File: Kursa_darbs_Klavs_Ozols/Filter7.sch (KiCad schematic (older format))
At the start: 11 parts, among them U9 TL074

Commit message: Shii ir 2. iteraacija kursa darbam!
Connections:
- net Audio4.5kHz: now also R42.1; no longer R42.2
- net at C36.1, R40.2, U9.1: now also R39.1; no longer R39.2
- net at C35.1, U9.2 (-): now also R39.2; no longer R39.1
- net at C37.1, U9.6 (-): now also R42.2; no longer R42.1
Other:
- moved on the sheet: R38, R41
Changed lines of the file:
@@
 L R R38
 U 1 1 5B01AED2
-P 2050 2500
-F 0 "R38" V 2130 2500 50  0000 C CNN
-F 1 "5.1k" V 2050 2500 50  0000 C CNN
-F 2 "" V 1980 2500 50  0001 C CNN
-F 3 "" H 2050 2500 50  0001 C CNN
-	1    2050 2500
+P 2050 2550
+F 0 "R38" V 2130 2550 50  0000 C CNN
+F 1 "5.1k" V 2050 2550 50  0000 C CNN
+F 2 "" V 1980 2550 50  0001 C CNN
+F 3 "" H 2050 2550 50  0001 C CNN
+	1    2050 2550
 	1    0    0    -1
 $EndComp
@@
 F 3 "" H 2750 2900 50  0001 C CNN
 	1    2750 2900
-	1    0    0    -1
+	0    1    1    0
 $EndComp
 Text HLabel 1450 2350 0    60   Input ~ 0
@@
 L R R41
 U 1 1 5B01B48F
-P 4400 2400
-F 0 "R41" V 4480 2400 50  0000 C CNN
-F 1 "5.1k" V 4400 2400 50  0000 C CNN
-F 2 "" V 4330 2400 50  0001 C CNN
-F 3 "" H 4400 2400 50  0001 C CNN
-	1    4400 2400
+P 4400 2450
+F 0 "R41" V 4480 2450 50  0000 C CNN
+F 1 "5.1k" V 4400 2450 50  0000 C CNN
+F 2 "" V 4330 2450 50  0001 C CNN
+F 3 "" H 4400 2450 50  0001 C CNN
+	1    4400 2450
 	1    0    0    -1
 $EndComp
@@
 F 3 "" H 5100 2800 50  0001 C CNN
 	1    5100 2800
-	1    0    0    -1
+	0    1    1    0
 $EndComp
 $Comp
@@
 	2550 3100 3700 3100
 Wire Wire Line
-	2750 3100 2750 3050
-Wire Wire Line
-	2250 3100 2050 3100
-Wire Wire Line
-	2050 3100 2050 2650
+	2750 3000 2750 3100
+Wire Wire Line
+	2050 3100 2250 3100
 Wire Wire Line
 	1950 2750 2250 2750
@@
 	4900 3000 6050 3000
 Wire Wire Line
-	5100 3000 5100 2950
-Wire Wire Line
-	4600 3000 4400 3000
-Wire Wire Line
-	4400 3000 4400 2550
+	5100 2900 5100 3000
+Wire Wire Line
+	4400 3000 4600 3000
 Wire Wire Line
 	4300 2650 4600 2650
@@
 	2300 2000 2300 2100
 Connection ~ 2300 2100
+Wire Wire Line
+	4400 2300 4400 2250
+Wire Wire Line
+	4400 2600 4400 3000
+Wire Wire Line
+	4950 2800 4950 2700
+Wire Wire Line
+	4950 2700 5100 2700
+Wire Wire Line
+	5100 2700 5100 2650
+Wire Wire Line
+	5250 2800 5250 2900
+Wire Wire Line
+	5250 2900 5100 2900
+Wire Wire Line
+	2600 2900 2600 2800
+Wire Wire Line
+	2600 2800 2750 2800
+Wire Wire Line
+	2750 2800 2750 2750
+Wire Wire Line
+	2900 2900 2900 3000
+Wire Wire Line
+	2900 3000 2750 3000
+Wire Wire Line
+	2050 2350 2050 2400
+Wire Wire Line
+	2050 2700 2050 3100
 $EndSCHEMATC

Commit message: Shii ir kursa darba 3. iteraacija
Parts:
- C35, C36, C37, C38: footprint (none) -> Capacitors_THT:C_Axial_L5.1mm_D3.1mm_P10.00mm_Horizontal
- R37, R38, R39, R40, R41, R42: footprint (none) -> Resistors_THT:R_Axial_DIN0309_L9.0mm_D3.2mm_P5.08mm_Vertical
- U9: footprint (none) -> TL074:DIL14
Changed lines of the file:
@@
 F 0 "U9" H 3250 2850 50  0000 L CNN
 F 1 "TL074" H 3250 2450 50  0000 L CNN
-F 2 "" H 3200 2750 50  0001 C CNN
+F 2 "TL074:DIL14" H 3200 2750 50  0001 C CNN
 F 3 "" H 3300 2850 50  0001 C CNN
 	1    3250 2650
@@
 F 0 "R37" V 1880 2750 50  0000 C CNN
 F 1 "6.8k" V 1800 2750 50  0000 C CNN
-F 2 "" V 1730 2750 50  0001 C CNN
-F 3 "" H 1800 2750 50  0001 C CNN
+F 2 "Resistors_THT:R_Axial_DIN0309_L9.0mm_D3.2mm_P5.08mm_Vertical" V 1730 2750 50  0001 C CNN
+F 3 "https://eu.mouser.com/datasheet/2/219/MOS-16613.pdf" H 1800 2750 50  0001 C CNN
 	1    1800 2750
 	0    1    1    0
@@
 F 0 "R38" V 2130 2550 50  0000 C CNN
 F 1 "5.1k" V 2050 2550 50  0000 C CNN
-F 2 "" V 1980 2550 50  0001 C CNN
-F 3 "" H 2050 2550 50  0001 C CNN
+F 2 "Resistors_THT:R_Axial_DIN0309_L9.0mm_D3.2mm_P5.08mm_Vertical" V 1980 2550 50  0001 C CNN
+F 3 "https://eu.mouser.com/datasheet/2/219/MOS-16613.pdf" H 2050 2550 50  0001 C CNN
 	1    2050 2550
 	1    0    0    -1
@@
 F 0 "C35" H 2425 2850 50  0000 L CNN
 F 1 "2.2nF" H 2425 2650 50  0000 L CNN
-F 2 "" H 2438 2600 50  0001 C CNN
-F 3 "" H 2400 2750 50  0001 C CNN
+F 2 "Capacitors_THT:C_Axial_L5.1mm_D3.1mm_P10.00mm_Horizontal" H 2438 2600 50  0001 C CNN
+F 3 "https://eu.mouser.com/datasheet/2/212/KEM_C1046_AXIAL_MOLDED_X7R-1145195.pdf" H 2400 2750 50  0001 C CNN
 	1    2400 2750
 	0    1    1    0
@@
 F 0 "C36" H 2425 3200 50  0000 L CNN
 F 1 "2.2nF" H 2425 3000 50  0000 L CNN
-F 2 "" H 2438 2950 50  0001 C CNN
-F 3 "" H 2400 3100 50  0001 C CNN
+F 2 "Capacitors_THT:C_Axial_L5.1mm_D3.1mm_P10.00mm_Horizontal" H 2438 2950 50  0001 C CNN
+F 3 "https://eu.mouser.com/datasheet/2/212/KEM_C1046_AXIAL_MOLDED_X7R-1145195.pdf" H 2400 3100 50  0001 C CNN
 	1    2400 3100
 	0    1    1    0
@@
 F 0 "R39" V 2830 2900 50  0000 C CNN
 F 1 "62k" V 2750 2900 50  0000 C CNN
-F 2 "" V 2680 2900 50  0001 C CNN
-F 3 "" H 2750 2900 50  0001 C CNN
+F 2 "Resistors_THT:R_Axial_DIN0309_L9.0mm_D3.2mm_P5.08mm_Vertical" V 2680 2900 50  0001 C CNN
+F 3 "https://eu.mouser.com/datasheet/2/219/MOS-16613.pdf" H 2750 2900 50  0001 C CNN
 	1    2750 2900
 	0    1    1    0
@@
 F 0 "R40" V 4230 2650 50  0000 C CNN
 F 1 "6.8k" V 4150 2650 50  0000 C CNN
-F 2 "" V 4080 2650 50  0001 C CNN
-F 3 "" H 4150 2650 50  0001 C CNN
+F 2 "Resistors_THT:R_Axial_DIN0309_L9.0mm_D3.2mm_P5.08mm_Vertical" V 4080 2650 50  0001 C CNN
+F 3 "https://eu.mouser.com/datasheet/2/219/MOS-16613.pdf" H 4150 2650 50  0001 C CNN
 	1    4150 2650
 	0    1    1    0
@@
 F 0 "R41" V 4480 2450 50  0000 C CNN
 F 1 "5.1k" V 4400 2450 50  0000 C CNN
-F 2 "" V 4330 2450 50  0001 C CNN
-F 3 "" H 4400 2450 50  0001 C CNN
+F 2 "Resistors_THT:R_Axial_DIN0309_L9.0mm_D3.2mm_P5.08mm_Vertical" V 4330 2450 50  0001 C CNN
+F 3 "https://eu.mouser.com/datasheet/2/219/MOS-16613.pdf" H 4400 2450 50  0001 C CNN
 	1    4400 2450
 	1    0    0    -1
@@
 F 0 "C37" H 4775 2750 50  0000 L CNN
 F 1 "2.2nF" H 4775 2550 50  0000 L CNN
-F 2 "" H 4788 2500 50  0001 C CNN
-F 3 "" H 4750 2650 50  0001 C CNN
+F 2 "Capacitors_THT:C_Axial_L5.1mm_D3.1mm_P10.00mm_Horizontal" H 4788 2500 50  0001 C CNN
+F 3 "https://eu.mouser.com/datasheet/2/212/KEM_C1046_AXIAL_MOLDED_X7R-1145195.pdf" H 4750 2650 50  0001 C CNN
 	1    4750 2650
 	0    1    1    0
@@
 F 0 "C38" H 4775 3100 50  0000 L CNN
 F 1 "2.2nF" H 4775 2900 50  0000 L CNN
-F 2 "" H 4788 2850 50  0001 C CNN
-F 3 "" H 4750 3000 50  0001 C CNN
+F 2 "Capacitors_THT:C_Axial_L5.1mm_D3.1mm_P10.00mm_Horizontal" H 4788 2850 50  0001 C CNN
+F 3 "https://eu.mouser.com/datasheet/2/212/KEM_C1046_AXIAL_MOLDED_X7R-1145195.pdf" H 4750 3000 50  0001 C CNN
 	1    4750 3000
 	0    1    1    0
@@
 F 0 "R42" V 5180 2800 50  0000 C CNN
 F 1 "62k" V 5100 2800 50  0000 C CNN
-F 2 "" V 5030 2800 50  0001 C CNN
-F 3 "" H 5100 2800 50  0001 C CNN
+F 2 "Resistors_THT:R_Axial_DIN0309_L9.0mm_D3.2mm_P5.08mm_Vertical" V 5030 2800 50  0001 C CNN
+F 3 "https://eu.mouser.com/datasheet/2/219/MOS-16613.pdf" H 5100 2800 50  0001 C CNN
 	1    5100 2800
 	0    1    1    0
@@
 F 0 "U9" H 5600 2750 50  0000 L CNN
 F 1 "TL074" H 5600 2350 50  0000 L CNN
-F 2 "" H 5550 2650 50  0001 C CNN
+F 2 "TL074:DIL14" H 5550 2650 50  0001 C CNN
 F 3 "" H 5650 2750 50  0001 C CNN
 	2    5600 2550

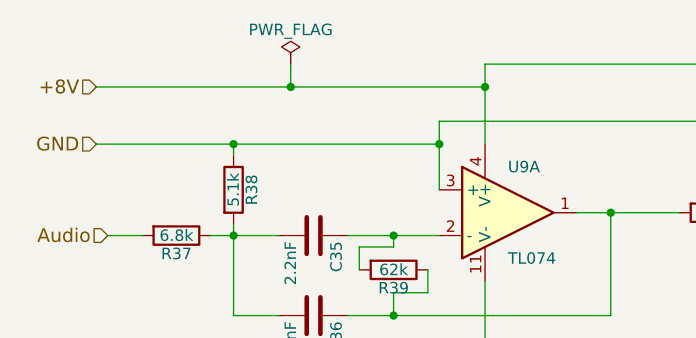
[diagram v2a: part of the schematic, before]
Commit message: Kursa darba plates 4. iteraacija
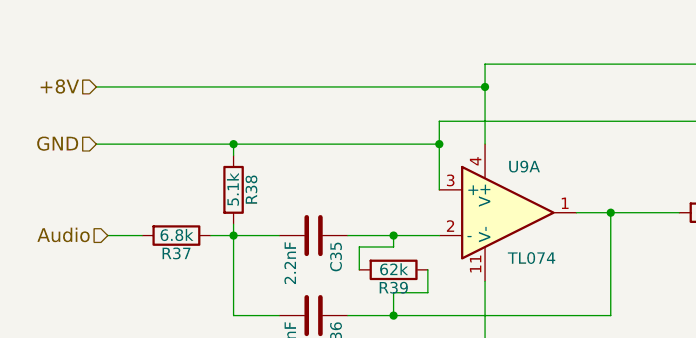
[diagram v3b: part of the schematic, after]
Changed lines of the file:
@@
 Text HLabel 6500 2550 2    60   Output ~ 0
 Audio4.5kHz
-$Comp
-L PWR_FLAG #FLG04
-U 1 1 5B046DF8
-P 2300 2000
-F 0 "#FLG04" H 2300 2075 50  0001 C CNN
-F 1 "PWR_FLAG" H 2300 2150 50  0000 C CNN
-F 2 "" H 2300 2000 50  0001 C CNN
-F 3 "" H 2300 2000 50  0001 C CNN
-	1    2300 2000
-	1    0    0    -1
-$EndComp
-Wire Wire Line
-	2300 2000 2300 2100
-Connection ~ 2300 2100
 Wire Wire Line
 	4400 2300 4400 2250

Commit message: Shiii ir 5. iteraacija manai platei - layouts
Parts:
- C35, C36, C37, C38: footprint Capacitors_THT:C_Axial_L5.1mm_D3.1mm_P10.00mm_Horizontal -> Capacitors_SMD:C_0805_HandSoldering
- R37, R38, R39, R40, R41, R42: footprint Resistors_THT:R_Axial_DIN0309_L9.0mm_D3.2mm_P5.08mm_Vertical -> Resistors_SMD:R_0805_HandSoldering
- U9: footprint TL074:DIL14 -> TL074:SO14
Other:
- moved on the sheet: C36, C38, R39, R42
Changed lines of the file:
@@
 EESchema Schematic File Version 2
+LIBS:Kursa_darbs_Klavs_Ozols-rescue
 LIBS:power
 LIBS:device
@@
 F 0 "U9" H 3250 2850 50  0000 L CNN
 F 1 "TL074" H 3250 2450 50  0000 L CNN
-F 2 "TL074:DIL14" H 3200 2750 50  0001 C CNN
+F 2 "TL074:SO14" H 3200 2750 50  0001 C CNN
 F 3 "" H 3300 2850 50  0001 C CNN
 	1    3250 2650
@@
 F 0 "R37" V 1880 2750 50  0000 C CNN
 F 1 "6.8k" V 1800 2750 50  0000 C CNN
-F 2 "Resistors_THT:R_Axial_DIN0309_L9.0mm_D3.2mm_P5.08mm_Vertical" V 1730 2750 50  0001 C CNN
-F 3 "https://eu.mouser.com/datasheet/2/219/MOS-16613.pdf" H 1800 2750 50  0001 C CNN
+F 2 "Resistors_SMD:R_0805_HandSoldering" V 1730 2750 50  0001 C CNN
+F 3 "https://eu.mouser.com/datasheet/2/219/RN73-11994.pdf" H 1800 2750 50  0001 C CNN
 	1    1800 2750
 	0    1    1    0
@@
 F 0 "R38" V 2130 2550 50  0000 C CNN
 F 1 "5.1k" V 2050 2550 50  0000 C CNN
-F 2 "Resistors_THT:R_Axial_DIN0309_L9.0mm_D3.2mm_P5.08mm_Vertical" V 1980 2550 50  0001 C CNN
-F 3 "https://eu.mouser.com/datasheet/2/219/MOS-16613.pdf" H 2050 2550 50  0001 C CNN
+F 2 "Resistors_SMD:R_0805_HandSoldering" V 1980 2550 50  0001 C CNN
+F 3 "https://eu.mouser.com/datasheet/2/219/RN73-11994.pdf" H 2050 2550 50  0001 C CNN
 	1    2050 2550
 	1    0    0    -1
@@
 F 0 "C35" H 2425 2850 50  0000 L CNN
 F 1 "2.2nF" H 2425 2650 50  0000 L CNN
-F 2 "Capacitors_THT:C_Axial_L5.1mm_D3.1mm_P10.00mm_Horizontal" H 2438 2600 50  0001 C CNN
-F 3 "https://eu.mouser.com/datasheet/2/212/KEM_C1046_AXIAL_MOLDED_X7R-1145195.pdf" H 2400 2750 50  0001 C CNN
+F 2 "Capacitors_SMD:C_0805_HandSoldering" H 2438 2600 50  0001 C CNN
+F 3 "https://eu.mouser.com/datasheet/2/427/vjcommercialseries-222796.pdf" H 2400 2750 50  0001 C CNN
 	1    2400 2750
 	0    1    1    0
@@
 L C C36
 U 1 1 5B01AF60
-P 2400 3100
-F 0 "C36" H 2425 3200 50  0000 L CNN
-F 1 "2.2nF" H 2425 3000 50  0000 L CNN
-F 2 "Capacitors_THT:C_Axial_L5.1mm_D3.1mm_P10.00mm_Horizontal" H 2438 2950 50  0001 C CNN
-F 3 "https://eu.mouser.com/datasheet/2/212/KEM_C1046_AXIAL_MOLDED_X7R-1145195.pdf" H 2400 3100 50  0001 C CNN
-	1    2400 3100
+P 2400 3350
+F 0 "C36" H 2425 3450 50  0000 L CNN
+F 1 "2.2nF" H 2425 3250 50  0000 L CNN
+F 2 "Capacitors_SMD:C_0805_HandSoldering" H 2438 3200 50  0001 C CNN
+F 3 "https://eu.mouser.com/datasheet/2/427/vjcommercialseries-222796.pdf" H 2400 3350 50  0001 C CNN
+	1    2400 3350
 	0    1    1    0
 $EndComp
@@
 L R R39
 U 1 1 5B01B098
-P 2750 2900
-F 0 "R39" V 2830 2900 50  0000 C CNN
-F 1 "62k" V 2750 2900 50  0000 C CNN
-F 2 "Resistors_THT:R_Axial_DIN0309_L9.0mm_D3.2mm_P5.08mm_Vertical" V 2680 2900 50  0001 C CNN
-F 3 "https://eu.mouser.com/datasheet/2/219/MOS-16613.pdf" H 2750 2900 50  0001 C CNN
-	1    2750 2900
-	0    1    1    0
+P 2750 3000
+F 0 "R39" V 2830 3000 50  0000 C CNN
+F 1 "62k" V 2750 3000 50  0000 C CNN
+F 2 "Resistors_SMD:R_0805_HandSoldering" V 2680 3000 50  0001 C CNN
+F 3 "https://eu.mouser.com/datasheet/2/219/RN73-11994.pdf" H 2750 3000 50  0001 C CNN
+	1    2750 3000
+	-1   0    0    1
 $EndComp
 Text HLabel 1450 2350 0    60   Input ~ 0
@@
 Text HLabel 1450 2100 0    60   Input ~ 0
 +8V
-Text HLabel 1500 3450 0    60   Input ~ 0
+Text HLabel 1500 3700 0    60   Input ~ 0
 -8V
 $Comp
@@
 F 0 "R40" V 4230 2650 50  0000 C CNN
 F 1 "6.8k" V 4150 2650 50  0000 C CNN
-F 2 "Resistors_THT:R_Axial_DIN0309_L9.0mm_D3.2mm_P5.08mm_Vertical" V 4080 2650 50  0001 C CNN
-F 3 "https://eu.mouser.com/datasheet/2/219/MOS-16613.pdf" H 4150 2650 50  0001 C CNN
+F 2 "Resistors_SMD:R_0805_HandSoldering" V 4080 2650 50  0001 C CNN
+F 3 "https://eu.mouser.com/datasheet/2/219/RN73-11994.pdf" H 4150 2650 50  0001 C CNN
 	1    4150 2650
 	0    1    1    0
@@
 F 0 "R41" V 4480 2450 50  0000 C CNN
 F 1 "5.1k" V 4400 2450 50  0000 C CNN
-F 2 "Resistors_THT:R_Axial_DIN0309_L9.0mm_D3.2mm_P5.08mm_Vertical" V 4330 2450 50  0001 C CNN
-F 3 "https://eu.mouser.com/datasheet/2/219/MOS-16613.pdf" H 4400 2450 50  0001 C CNN
+F 2 "Resistors_SMD:R_0805_HandSoldering" V 4330 2450 50  0001 C CNN
+F 3 "https://eu.mouser.com/datasheet/2/219/RN73-11994.pdf" H 4400 2450 50  0001 C CNN
 	1    4400 2450
 	1    0    0    -1
@@
 F 0 "C37" H 4775 2750 50  0000 L CNN
 F 1 "2.2nF" H 4775 2550 50  0000 L CNN
-F 2 "Capacitors_THT:C_Axial_L5.1mm_D3.1mm_P10.00mm_Horizontal" H 4788 2500 50  0001 C CNN
-F 3 "https://eu.mouser.com/datasheet/2/212/KEM_C1046_AXIAL_MOLDED_X7R-1145195.pdf" H 4750 2650 50  0001 C CNN
+F 2 "Capacitors_SMD:C_0805_HandSoldering" H 4788 2500 50  0001 C CNN
+F 3 "https://eu.mouser.com/datasheet/2/427/vjcommercialseries-222796.pdf" H 4750 2650 50  0001 C CNN
 	1    4750 2650
 	0    1    1    0
@@
 L C C38
 U 1 1 5B01B49B
-P 4750 3000
-F 0 "C38" H 4775 3100 50  0000 L CNN
-F 1 "2.2nF" H 4775 2900 50  0000 L CNN
-F 2 "Capacitors_THT:C_Axial_L5.1mm_D3.1mm_P10.00mm_Horizontal" H 4788 2850 50  0001 C CNN
-F 3 "https://eu.mouser.com/datasheet/2/212/KEM_C1046_AXIAL_MOLDED_X7R-1145195.pdf" H 4750 3000 50  0001 C CNN
-	1    4750 3000
+P 4750 3250
+F 0 "C38" H 4775 3350 50  0000 L CNN
+F 1 "2.2nF" H 4775 3150 50  0000 L CNN
+F 2 "Capacitors_SMD:C_0805_HandSoldering" H 4788 3100 50  0001 C CNN
+F 3 "https://eu.mouser.com/datasheet/2/427/vjcommercialseries-222796.pdf" H 4750 3250 50  0001 C CNN
+	1    4750 3250
 	0    1    1    0
 $EndComp
@@
 L R R42
 U 1 1 5B01B4A1
-P 5100 2800
-F 0 "R42" V 5180 2800 50  0000 C CNN
-F 1 "62k" V 5100 2800 50  0000 C CNN
-F 2 "Resistors_THT:R_Axial_DIN0309_L9.0mm_D3.2mm_P5.08mm_Vertical" V 5030 2800 50  0001 C CNN
-F 3 "https://eu.mouser.com/datasheet/2/219/MOS-16613.pdf" H 5100 2800 50  0001 C CNN
-	1    5100 2800
-	0    1    1    0
+P 5100 2900
+F 0 "R42" V 5180 2900 50  0000 C CNN
+F 1 "62k" V 5100 2900 50  0000 C CNN
+F 2 "Resistors_SMD:R_0805_HandSoldering" V 5030 2900 50  0001 C CNN
+F 3 "https://eu.mouser.com/datasheet/2/219/RN73-11994.pdf" H 5100 2900 50  0001 C CNN
+	1    5100 2900
+	-1   0    0    1
 $EndComp
 $Comp
@@
 F 0 "U9" H 5600 2750 50  0000 L CNN
 F 1 "TL074" H 5600 2350 50  0000 L CNN
-F 2 "TL074:DIL14" H 5550 2650 50  0001 C CNN
+F 2 "TL074:SO14" H 5550 2650 50  0001 C CNN
 F 3 "" H 5650 2750 50  0001 C CNN
 	2    5600 2550
 	1    0    0    -1
 $EndComp
+Text HLabel 6500 2550 2    60   Output ~ 0
+Audio4.5kHz
 Wire Wire Line
 	2550 2750 2950 2750
-Connection ~ 2750 2750
-Wire Wire Line
-	2550 3100 3700 3100
-Wire Wire Line
-	2750 3000 2750 3100
-Wire Wire Line
-	2050 3100 2250 3100
+Wire Wire Line
+	3700 3350 2550 3350
+Wire Wire Line
+	2750 3150 2750 3350
+Wire Wire Line
+	2050 3350 2250 3350
 Wire Wire Line
 	1950 2750 2250 2750
@@
 	1450 2100 3150 2100
 Wire Wire Line
-	1500 3450 3150 3450
-Wire Wire Line
-	3150 3450 3150 2950
+	3150 3700 1500 3700
+Wire Wire Line
+	3150 2950 3150 3700
 Wire Wire Line
 	3550 2650 4000 2650
 Wire Wire Line
-	3700 3100 3700 2650
-Connection ~ 2750 3100
+	3700 2650 3700 3350
+Connection ~ 2750 3350
 Connection ~ 3700 2650
 Wire Wire Line
 	4900 2650 5300 2650
-Connection ~ 5100 2650
-Wire Wire Line
-	4900 3000 6050 3000
-Wire Wire Line
-	5100 2900 5100 3000
-Wire Wire Line
-	4400 3000 4600 3000
 Wire Wire Line
 	4300 2650 4600 2650
@@
 	3150 2000 5500 2000
 Wire Wire Line
-	3150 3350 5500 3350
-Wire Wire Line
-	5500 3350 5500 2850
+	5500 3600 3150 3600
+Wire Wire Line
+	5500 2850 5500 3600
 Wire Wire Line
 	5900 2550 6500 2550
 Wire Wire Line
-	6050 3000 6050 2550
-Connection ~ 5100 3000
+	6050 2550 6050 3250
 Connection ~ 6050 2550
-Connection ~ 3150 3350
+Connection ~ 3150 3600
 Connection ~ 2950 2350
 Connection ~ 3150 2100
-Text HLabel 6500 2550 2    60   Output ~ 0
-Audio4.5kHz
 Wire Wire Line
 	4400 2300 4400 2250
 Wire Wire Line
-	4400 2600 4400 3000
-Wire Wire Line
-	4950 2800 4950 2700
-Wire Wire Line
-	4950 2700 5100 2700
-Wire Wire Line
-	5100 2700 5100 2650
-Wire Wire Line
-	5250 2800 5250 2900
-Wire Wire Line
-	5250 2900 5100 2900
-Wire Wire Line
-	2600 2900 2600 2800
-Wire Wire Line
-	2600 2800 2750 2800
-Wire Wire Line
-	2750 2800 2750 2750
-Wire Wire Line
-	2900 2900 2900 3000
-Wire Wire Line
-	2900 3000 2750 3000
+	4400 2600 4400 3250
 Wire Wire Line
 	2050 2350 2050 2400
 Wire Wire Line
-	2050 2700 2050 3100
+	2050 2700 2050 3350
+Wire Wire Line
+	5100 2750 5100 2650
+Connection ~ 5100 2650
+Wire Wire Line
+	4400 3250 4600 3250
+Wire Wire Line
+	6050 3250 4900 3250
+Wire Wire Line
+	5100 3050 5100 3250
+Connection ~ 5100 3250
+Wire Wire Line
+	2750 2850 2750 2750
+Connection ~ 2750 2750
 $EndSCHEMATC
